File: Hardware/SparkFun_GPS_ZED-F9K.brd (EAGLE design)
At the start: 25.4 x 25.4 mm, 35 parts, among them J4 U.FL, Y1 32.768kHz

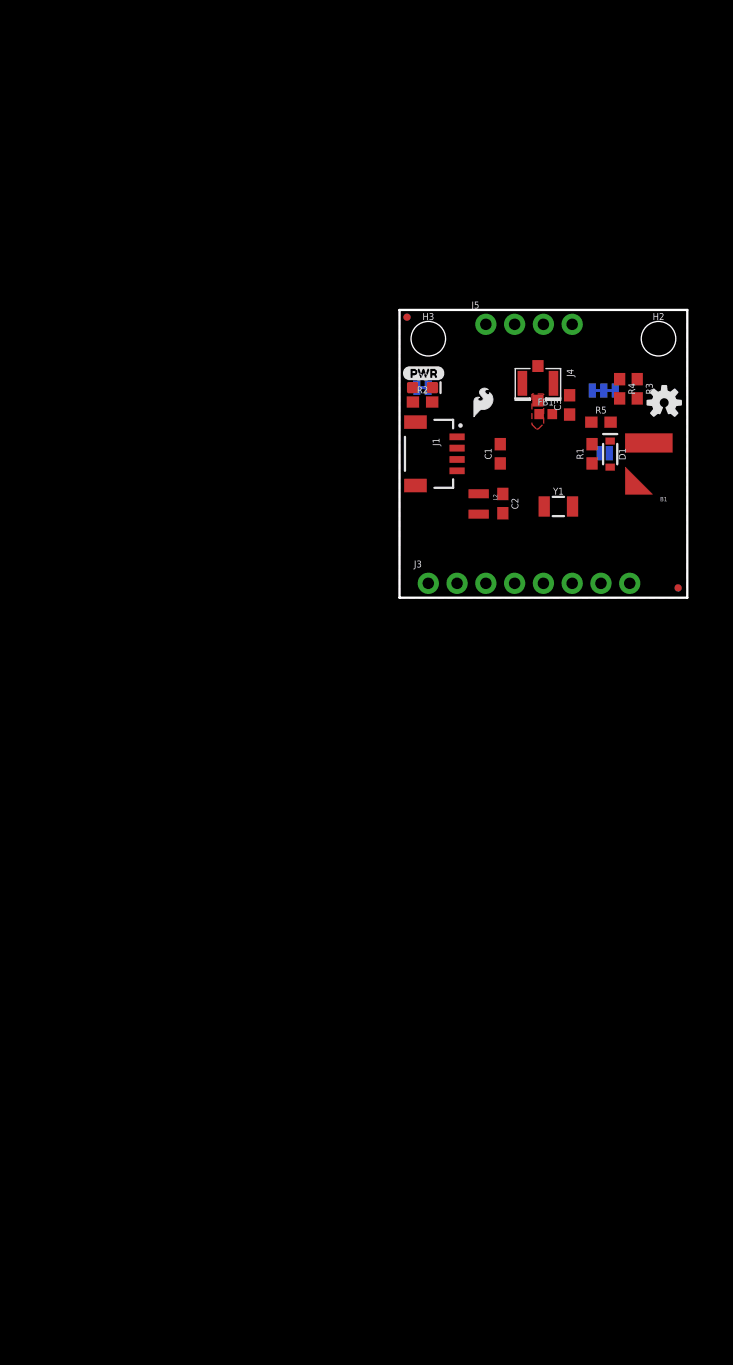
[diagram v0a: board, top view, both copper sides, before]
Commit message: Adds circuitry for active antenna or RF_IN
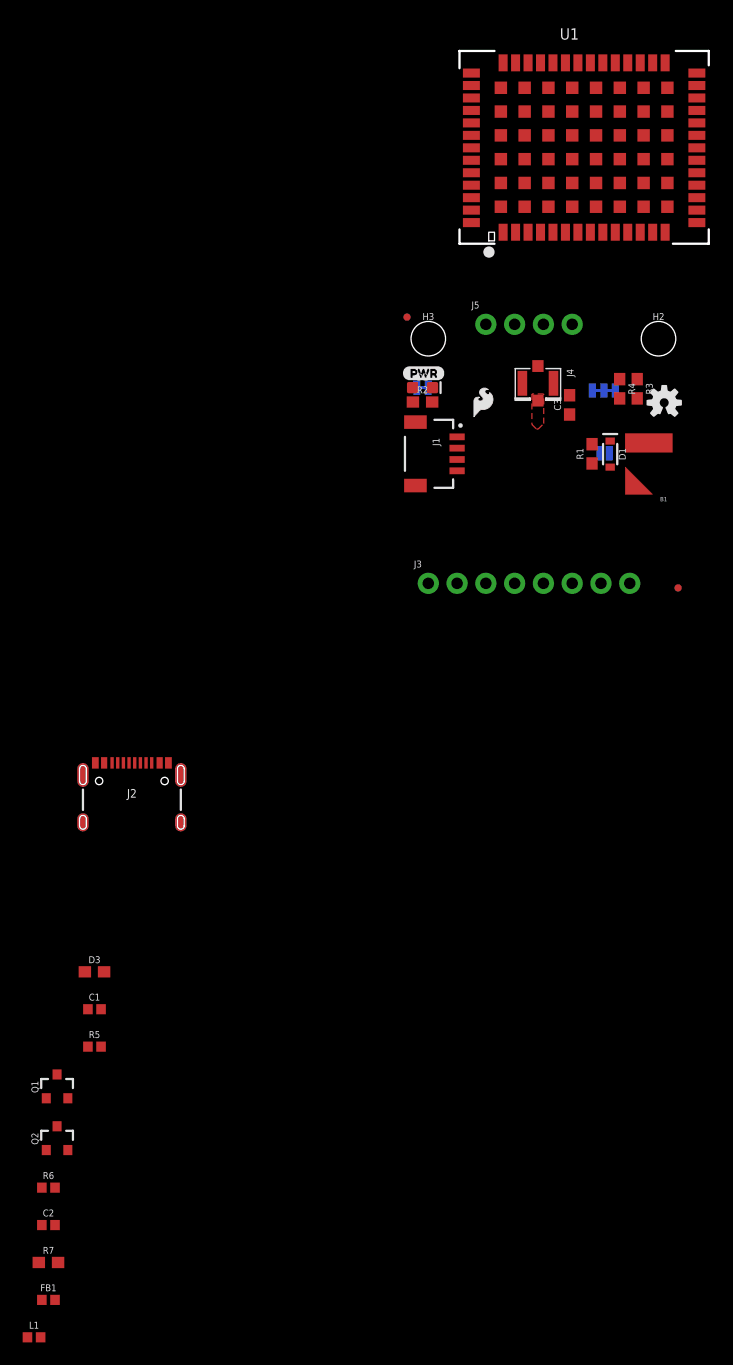
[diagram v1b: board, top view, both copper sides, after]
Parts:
- removed FRAME1: FRAME-LETTER, SparkFun-Aesthetics:CREATIVE_COMMONS
- removed L2: 2.2uH, SparkFun-Coils:0806
- removed Y1: 32.768kHz, SparkFun-Clocks:CRYSTAL-SMD-3.2X1.5MM
- added D3: 24V, SparkFun-DiscreteSemi:0603
- added FRAME2: FRAME-LEDGER, SparkFun-Aesthetics:CREATIVE_COMMONS
- added J2: (no value), SparkFun-Connectors:USB-C-16P
- added L1: 3.9NH, SparkFun-Coils:0402
- added Q1, Q2: 600mA/40V, SparkFun-DiscreteSemi:SOT23-3
- added R6: 22, SparkFun-Resistors:0402
- added R7: 10, SparkFun-Resistors:0603
- added U1: UBLOX_ZED_F9K, classified:UBLOX_ZED_F9K
- C1: value 4.7uF -> 0.1uF; device SparkFun-Capacitors:0603 -> SparkFun-Capacitors:0402
- C2: value 0.1uF -> 1.0uF; device SparkFun-Capacitors:0603 -> SparkFun-Capacitors:0402
- FB1: value FERRITE_BEAD-120_OHM-0402 -> FERRITE_BEAD
- R5: value 10 -> 2.2KOHM-0402-1/16W-1%; device SparkFun-Resistors:0603 -> SparkFun-Resistors:0402
- moved FB1 89.7 mm to (-31.0, -62.0)
- moved C2 75.3 mm to (-31.0, -55.4), turned to 0 degrees
- moved R5 71.0 mm to (-26.9, -39.6)
- moved C1 60.7 mm to (-26.9, -36.3), turned to 0 degrees
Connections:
- removed net ANT: FB1.1, J4.FEED
- new net N$10: C1.1, L1.1, Q1.2
- new net N$11: Q2.2, R6.1
- new net N$5: C2.2, FB1.2, R6.2, R7.1
- new net N$6: Q1.1, Q2.3, R5.1
- new net N$7: C3.2, D3.2, J4.FEED, L1.2
- new net RF_IN: C3.1, U1.P2
- new net V_USB: U1.P38
- net 3.3V: now also FB1.1, U1.P33, U1.P34; no longer R5.2
- net GND: now also C1.2, C2.1, D3.1, R5.2, U1.G1, U1.G10, U1.G11, U1.G12, U1.G13, U1.G14, U1.G15, U1.G16, U1.G17, U1.G18, U1.G19, U1.G2, U1.G20, U1.G21, U1.G22, U1.G23, U1.G24, U1.G25, U1.G26, U1.G27, U1.G28, U1.G29, U1.G3, U1.G30, U1.G31, U1.G32, U1.G33, U1.G34, U1.G35, U1.G36, U1.G37, U1.G38, U1.G39, U1.G4, U1.G40, U1.G41, U1.G42, U1.G43, U1.G44, U1.G45, U1.G46, U1.G47, U1.G48, U1.G5, U1.G6, U1.G7, U1.G8, U1.G9, U1.P1, U1.P12, U1.P14, U1.P3, U1.P32, U1.P37, U1.P41, U1.P48; no longer C3.2
- net N$9: now also Q1.3, Q2.1, R7.2; no longer C3.1, FB1.2, R5.1
- net V_BATT: now also U1.P36
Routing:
- removed copper zone on layer 1, net GND
- removed copper zone on layer 16, net GND
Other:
- board size 25.4 x 25.4 mm -> 22 x 17 mm

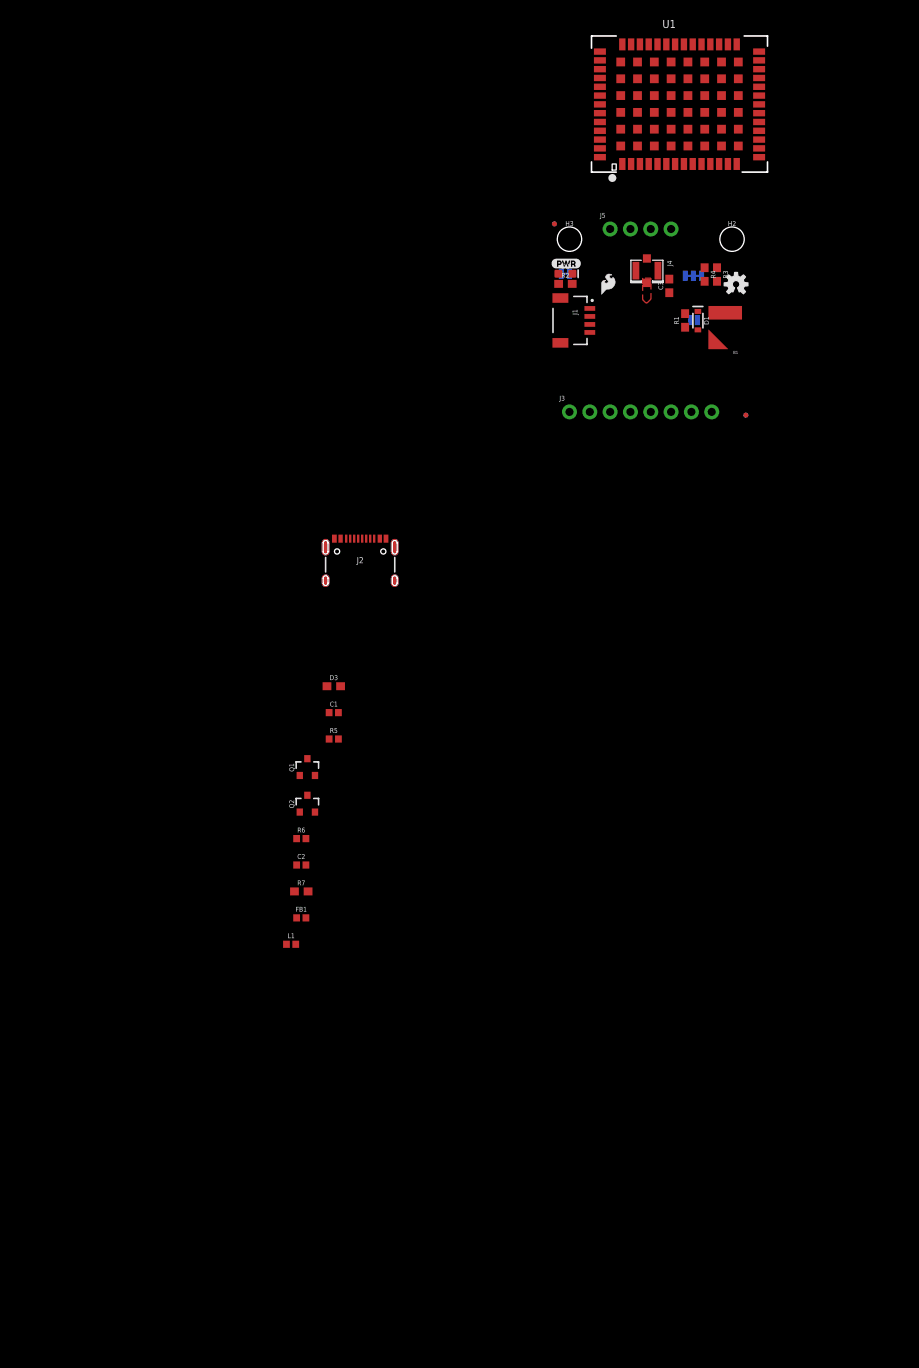
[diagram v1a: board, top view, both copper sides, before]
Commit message: Adds power circuitry with ESD protection, adds LEDs
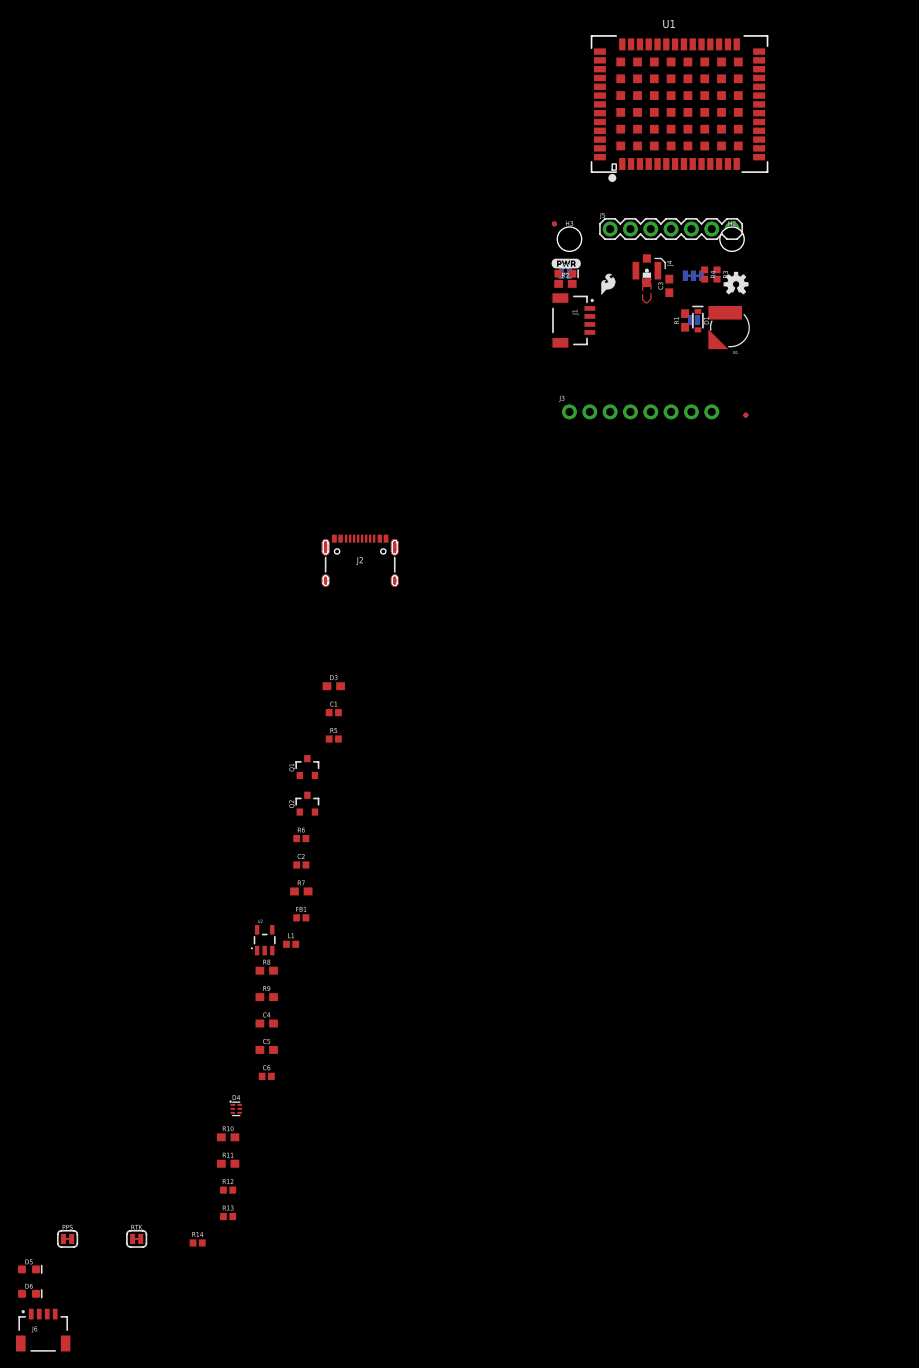
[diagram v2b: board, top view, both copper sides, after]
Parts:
- added C4, C5: 1.0uF, SparkFun-Capacitors:0603
- added C6: 1.0uF, SparkFun-Capacitors:0402
- added D4: PRTR5V0U2F, SparkFun-IC-Power:SOT886
- added D5, D6: BLUE, SparkFun-LED:LED-0603
- added J6: QWIIC_RIGHT_ANGLE, SparkFun-Connectors:JST04_1MM_RA
- added PPS, RTK: JUMPER-SMT_2_NC_TRACE_SILK, SparkFun-Jumpers:SMT-JUMPER_2_NC_TRACE_SILK
- added R10, R11: 27, SparkFun-Resistors:0603
- added R12: 100K, SparkFun-Resistors:0402
- added R13, R14: 1KOHM-0402-1/16W-1%, SparkFun-Resistors:0402
- added R8, R9: 5.1k, SparkFun-Resistors:0603
- added U2: 3.3V, SparkFun-IC-Power:SOT23-5
- J1: value (none) -> QWIIC_RIGHT_ANGLE
- J5: device SparkFun-Connectors:1X04_NO_SILK -> SparkFun-Connectors:1X07
- R3, R4: value 2.2k -> 2.2K; device SparkFun-Resistors:0603 -> SparkFun-Resistors:0402
- R5: value 2.2KOHM-0402-1/16W-1% -> 2.2K
- renumbered JP4 to PWR
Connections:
- removed net SDA/CS: J1.3, J3.8, R3.1
- removed net TIMEPULSE: J5.3
- removed net V_USB: U1.P38
- new net DIR: J5.7, U1.P23
- new net DMINUS: R11.2, U1.P39
- new net DPLUS: R10.2, U1.P40
- new net INT: U1.P51
- new net N$14: J2.B5, R8.2
- new net N$15: J2.A5, R9.2
- new net N$16: D4.5, R10.1
- new net N$17: D4.4, R11.1
- new net N$20: D4.2, J2.A6, J2.B6
- new net N$21: D4.3, J2.A7, J2.B7
- new net N$22: R14.1, RTK.2
- new net N$23: PPS.2, R13.1
- new net N$24: D5.C, R13.2
- new net N$25: D6.C, R14.2
- new net PPS: D5.A, J5.3, U1.P53
- new net RTK_STAT: D6.A, U1.P20
- new net RXI2: U1.P26
- new net SDA/!CS: J1.3, J3.8, J6.3, R3.1, U1.P44
- new net SHLD: J2.SHLD1, J2.SHLD2, J2.SHLD3, J2.SHLD4, J2.SHLD5, J2.SHLD6, J2.SHLD7, J2.SHLD8
- new net TXO2: U1.P27
- new net TX_READY: J5.5, U1.P46
- new net VIN: D4.1, J2.VBUS1, J2.VBUS2, J3.4
- new net VOUT: C4.1, D4.6, U2.1, U2.3
- new net WT: J5.6, U1.P22
- net !RESET: now also U1.P49
- net !SAFEBOOT: now also U1.P50
- net 3.3V: now also C5.1, C6.1, D2.A, J6.2, R12.2, U1.P38, U2.5; no longer J3.4, R2.2
- net D_SEL: now also U1.P47
- net GND: now also C4.2, C5.2, C6.2, J2.GND, J2.GND2, J6.1, PPS.1, R12.1, R8.1, R9.1, RTK.1, U2.2
- net N$4: now also D2.C, R2.2; no longer D2.A, R2.1
- net N$8: now also R2.1; no longer D2.C
- net RXI/MOSI: now also U1.P43
- net SCL/CLK: now also J6.4, U1.P45
- net TXO/MISO: now also U1.P42

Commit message: Adds I/O protection to INPUTS using new part, removes active antenna circuitry in place of VCC bias for external patch active antennas
* Localizes parts into a rough shape for final product
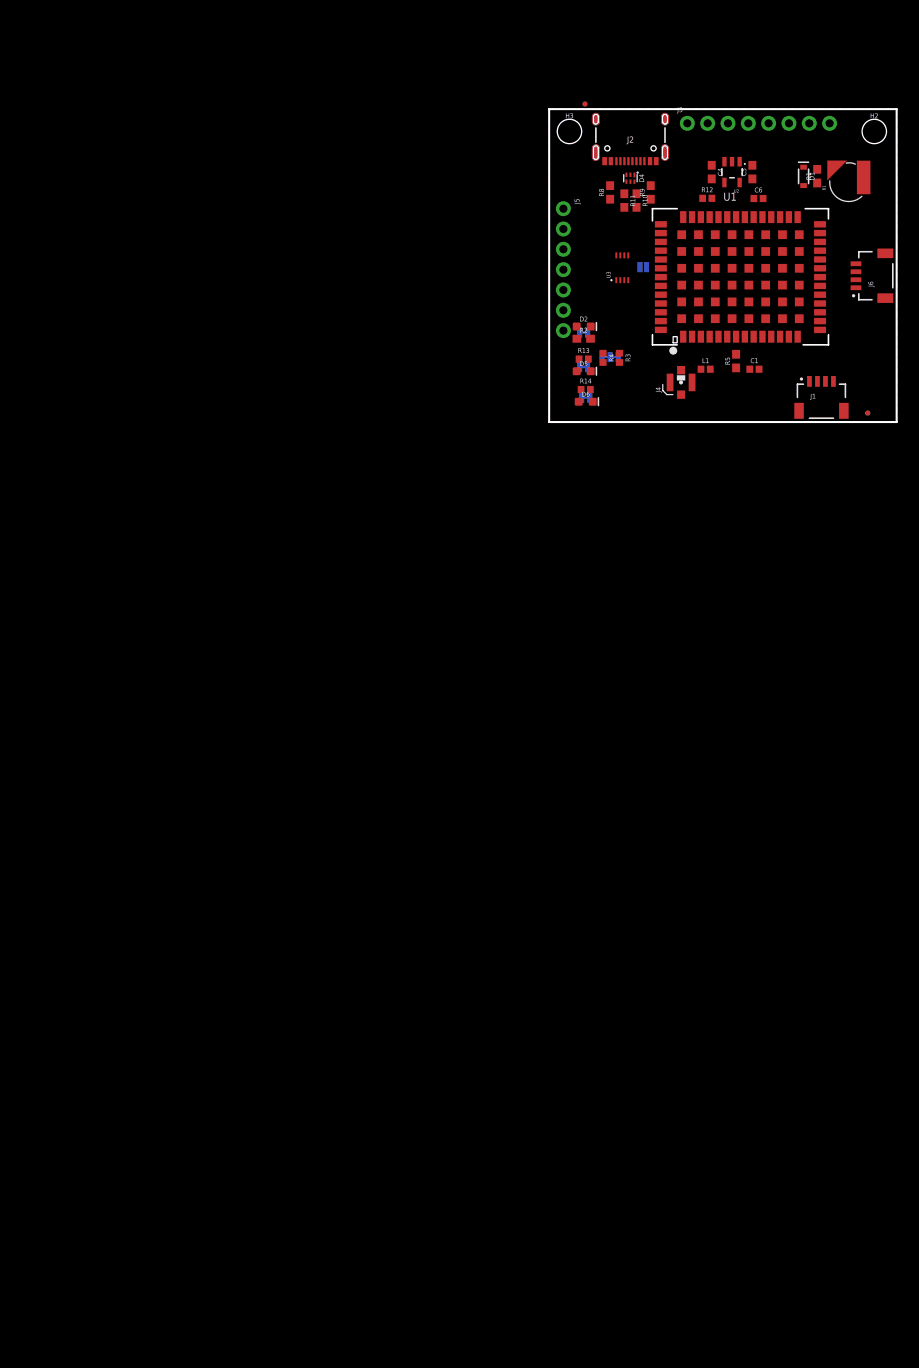
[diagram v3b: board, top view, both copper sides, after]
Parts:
- removed C2: 1.0uF, SparkFun-Capacitors:0402
- removed C3: 47pF, SparkFun-Capacitors:0603
- removed D3: 24V, SparkFun-DiscreteSemi:0603
- removed FB1: FERRITE_BEAD, SparkFun-Coils:0402
- removed LOGO1: SFE_LOGO_NAME_FLAME.1_INCH, SparkFun-Aesthetics:SFE_LOGO_NAME_FLAME_.1
- removed LOGO2: OSHW-LOGOS, SparkFun-Aesthetics:OSHW-LOGO-S
- removed LOGO3: SFE_LOGO_FLAME.1_INCH, SparkFun-Aesthetics:SFE_LOGO_FLAME_.1
- removed Q1, Q2: 600mA/40V, SparkFun-DiscreteSemi:SOT23-3
- removed R6: 22, SparkFun-Resistors:0402
- removed R7: 10, SparkFun-Resistors:0603
- removed U$17: (no value), SPI_JUMPER:SPI0
- removed U$25: (no value), LED:LED0
- removed U$26: (no value), Labels:PWR-()-03
- removed U$36: (no value), Labels:QWIIC_COPYRIGHT_SMALL
- added U3: TRIPLE_BUFFER_74LVC3G07, classified:SOP_8-PIN
- J5: device SparkFun-Connectors:1X07 -> SparkFun-Connectors:1X07_NO_SILK
- R5: value 2.2K -> 20; device SparkFun-Resistors:0402 -> SparkFun-Resistors:0603
- moved J6 164.8 mm to (38.4, 18.3), turned to 90 degrees
- moved R12 137.7 mm to (19.8, 28.0)
- moved D5 132.0 mm to (4.32, 6.35)
- moved D6 131.4 mm to (4.57, 2.54)
- moved R11 130.2 mm to (9.40, 27.7), turned to 270 degrees
- moved R10 127.7 mm to (10.9, 27.7), turned to 270 degrees
- moved PPS 126.6 mm to (4.32, 6.86), flipped to the bottom
- moved D4 126.3 mm to (10.2, 30.5), turned to 270 degrees
- moved C6 125.8 mm to (26.2, 27.9)
- moved C5 125.4 mm to (25.4, 31.2), turned to 90 degrees
- moved C4 120.1 mm to (20.3, 31.2), turned to 270 degrees
- moved RTK 119.2 mm to (4.57, 3.05), flipped to the bottom
- moved R14 117.2 mm to (4.57, 4.06)
- moved R13 116.0 mm to (4.32, 7.87)
- moved U2 112.4 mm to (22.9, 31.2), turned to 180 degrees
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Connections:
- removed net !INT: J5.1
- removed net !RESET: J5.2, U1.P49
- removed net !SAFEBOOT: J5.4, U1.P50
- removed net INT: U1.P51
- removed net N$10: C1.1, L1.1, Q1.2
- removed net N$11: Q2.2, R6.1
- removed net N$20: D4.2, J2.A6, J2.B6
- removed net N$21: D4.3, J2.A7, J2.B7
- removed net N$9: Q1.3, Q2.1, R7.2
- removed net VOUT: C4.1, D4.6, U2.1, U2.3
- new net !RESET_IN: U1.P49, U3.P1
- new net !RESET_OUT: J5.2, U3.P7
- new net !SAFEBOOT_IN: U1.P50, U3.P6
- new net !SAFEBOOT_OUT: J5.4, U3.P2
- new net INT_IN: U1.P51, U3.P3
- new net INT_OUT: J5.1, U3.P5
- new net V_RF: R5.2, U1.P7
- new net V_USB: D4.1, J2.VBUS1, J2.VBUS2
- net 3.3V: now also U3.P8; no longer FB1.1
- net DMINUS: now also R10.2; no longer R11.2
- net DPLUS: now also R11.2; no longer R10.2
- net GND: now also U3.P4; no longer C2.1, D3.1, R5.2
- net N$5: now also C1.1, L1.2, R5.1; no longer C2.2, FB1.2, R6.2, R7.1
- net N$6: now also D4.3, J2.A6, J2.B6; no longer Q1.1, Q2.3, R5.1
- net N$7: now also D4.2, J2.A7, J2.B7; no longer C3.2, D3.2, J4.FEED, L1.2
- net RF_IN: now also J4.FEED, L1.1; no longer C3.1
- net VIN: now also C4.1, D4.6, U2.1, U2.3; no longer D4.1, J2.VBUS1, J2.VBUS2
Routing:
- added copper zone on layer 1, net GND
- added copper zone on layer 16, net GND
- removed copper zone on layer 1, net ANT
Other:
- board size 22 x 17 mm -> 43.4 x 39.1 mm
- board text removed: "Units in Inches"

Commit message: Just some light trace work to get a feel for layout
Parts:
- moved C4 0.25 mm to (20.3, 31.0)
- moved C5 0.25 mm to (25.4, 31.0)
- moved C6 0.25 mm to (26.2, 28.2)
- moved R12 0.25 mm to (19.5, 28.0)
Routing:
- net 3.3V: track 0.00 -> 18.1 mm
- net V_BATT: track 0.00 -> 17.2 mm, vias 0 -> 2
- net VIN: track 0.00 -> 10.3 mm
- net N$2: track 0.00 -> 1.82 mm

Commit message: Solidifies breakout board size
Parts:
- added H1, H4: STAND-OFFTIGHT, SparkFun-Hardware:STAND-OFF-TIGHT
- added J8: (no value), SparkFun-Connectors:1X09_NO_SILK
- J3: device SparkFun-Connectors:1X08_NO_SILK -> SparkFun-Connectors:1X06_NO_SILK
- J5: device SparkFun-Connectors:1X07_NO_SILK -> SparkFun-Connectors:1X06_NO_SILK
- R2: value 1k -> 1KOHM-0402-1/16W-1%; device SparkFun-Resistors:0603 -> SparkFun-Resistors:0402
- R8, R9: device SparkFun-Resistors:0603 -> SparkFun-Resistors:0402
- moved J1 41.1 mm to (5.08, 34.3), turned to 270 degrees
- moved J5 35.9 mm to (34.3, 41.9), turned to 180 degrees
- moved FD1 32.4 mm to (36.8, 39.4)
- moved FD3 32.4 mm to (36.8, 39.4)
- moved RTK 29.9 mm to (34.4, 1.78)
- moved R14 29.8 mm to (34.3, 1.27)
- moved D6 29.7 mm to (34.3, 2.54)
- moved J3 25.9 mm to (41.9, 29.2), turned to 270 degrees
- moved R13 25.8 mm to (29.2, 1.27)
- moved PPS 25.4 mm to (29.2, 1.73)
- moved D5 25.2 mm to (29.2, 2.54)
- moved PWR 22.4 mm to (24.6, 1.78)
- moved D2 21.9 mm to (24.1, 2.54), turned to 180 degrees
- moved R2 21.8 mm to (24.1, 1.27), turned to 180 degrees
- moved JP2 18.0 mm to (7.62, 26.2)
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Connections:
- new net !CS: J3.3
- new net SCK: J3.6
- net !RESET_OUT: now also J8.2; no longer J5.2
- net !SAFEBOOT_IN: now also J8.3
- net !SAFEBOOT_OUT: no longer J5.4
- net 3.3V: now also J8.7
- net DIR: no longer J5.7
- net GND: now also J3.1, J5.1, J8.6; no longer J3.6
- net INT_OUT: now also J8.4; no longer J5.1
- net PPS: now also J8.1; no longer J5.3
- net RXI/MOSI: now also J3.4; no longer J3.3
- net RXI2: now also J5.4
- net SCL/CLK: now also J8.9; no longer J3.7
- net SDA/!CS: now also J8.8; no longer J3.8
- net TXO/MISO: now also J3.5; no longer J3.2
- net TXO2: now also J5.5
- net TX_READY: now also J8.5; no longer J5.5
- net VIN: now also J3.2; no longer J3.4
- net WT: no longer J5.6
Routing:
- net 3.3V: track 18.1 -> 51.5 mm, vias 0 -> 2
- net V_BATT: track 17.2 -> 0.00 mm, vias 2 -> 0
- net V_USB: track 0.00 -> 9.23 mm, vias 0 -> 2
- net DMINUS: track 0.00 -> 8.61 mm
- net DPLUS: track 0.00 -> 8.49 mm
- net N$15: track 0.00 -> 7.04 mm
- net N$14: track 0.00 -> 6.54 mm
- net N$6: track 0.00 -> 5.00 mm
- net VIN: track 10.3 -> 15.2 mm
- net N$7: track 0.00 -> 3.83 mm
- net N$16: track 0.00 -> 2.46 mm
- net N$17: track 0.00 -> 2.41 mm
- net N$2: track 1.82 -> 0.00 mm
- added copper zone on layer 1, net SHIELD
- added copper zone on layer 16, net SHIELD
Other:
- board size 43.4 x 39.1 mm -> 43.2 x 43.2 mm
